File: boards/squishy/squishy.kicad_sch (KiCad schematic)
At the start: 69 parts, among them J10 QXH-060, J2 Conn_02x20_Odd_Even_Shielded, J3 MEM2061-01-188-00-A, J8 TRIGGER, J9 REFCLK, SW2 DFU, U1 LFE5UM5G-45F-8BG381C, U2 GD25Q64EWIGR, U6 ATSAMD09D14A-M, X1 48MHz

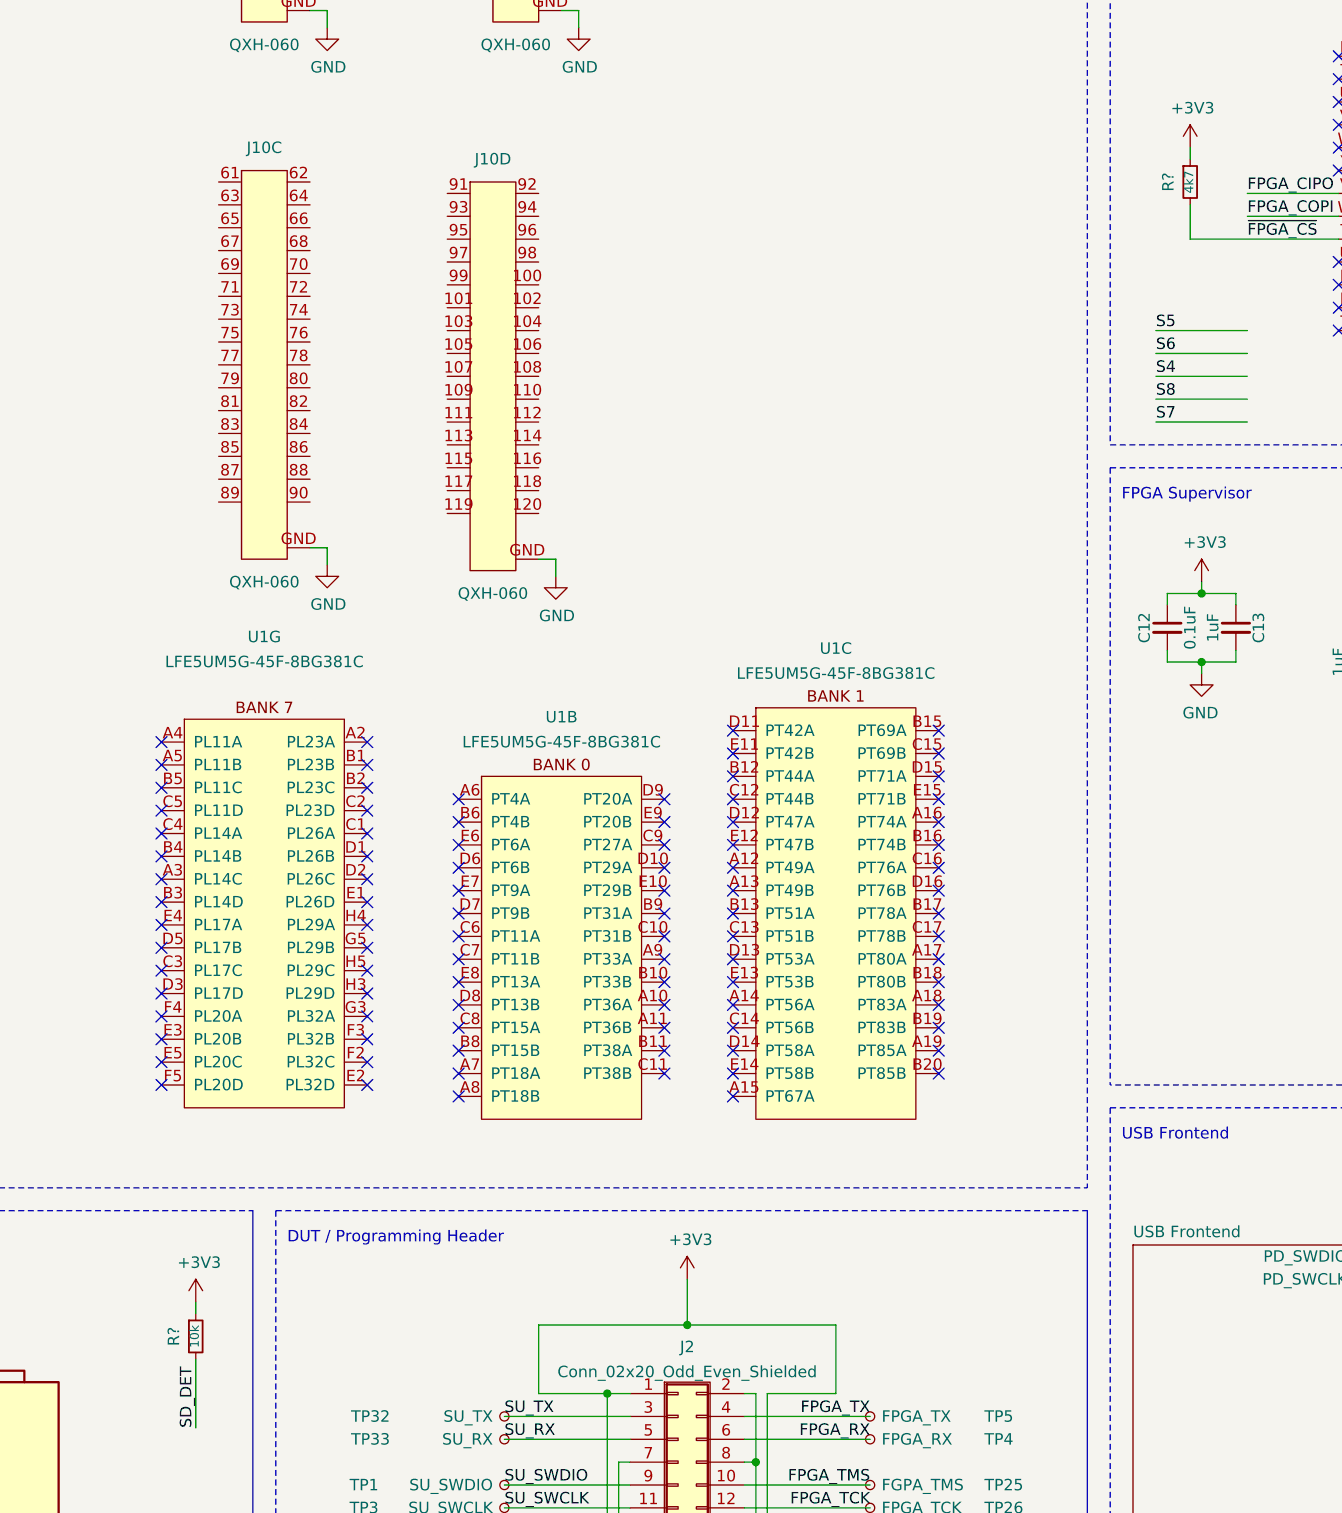
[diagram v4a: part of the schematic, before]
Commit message: hardware: squishy: some footprint/part updates and cleanup
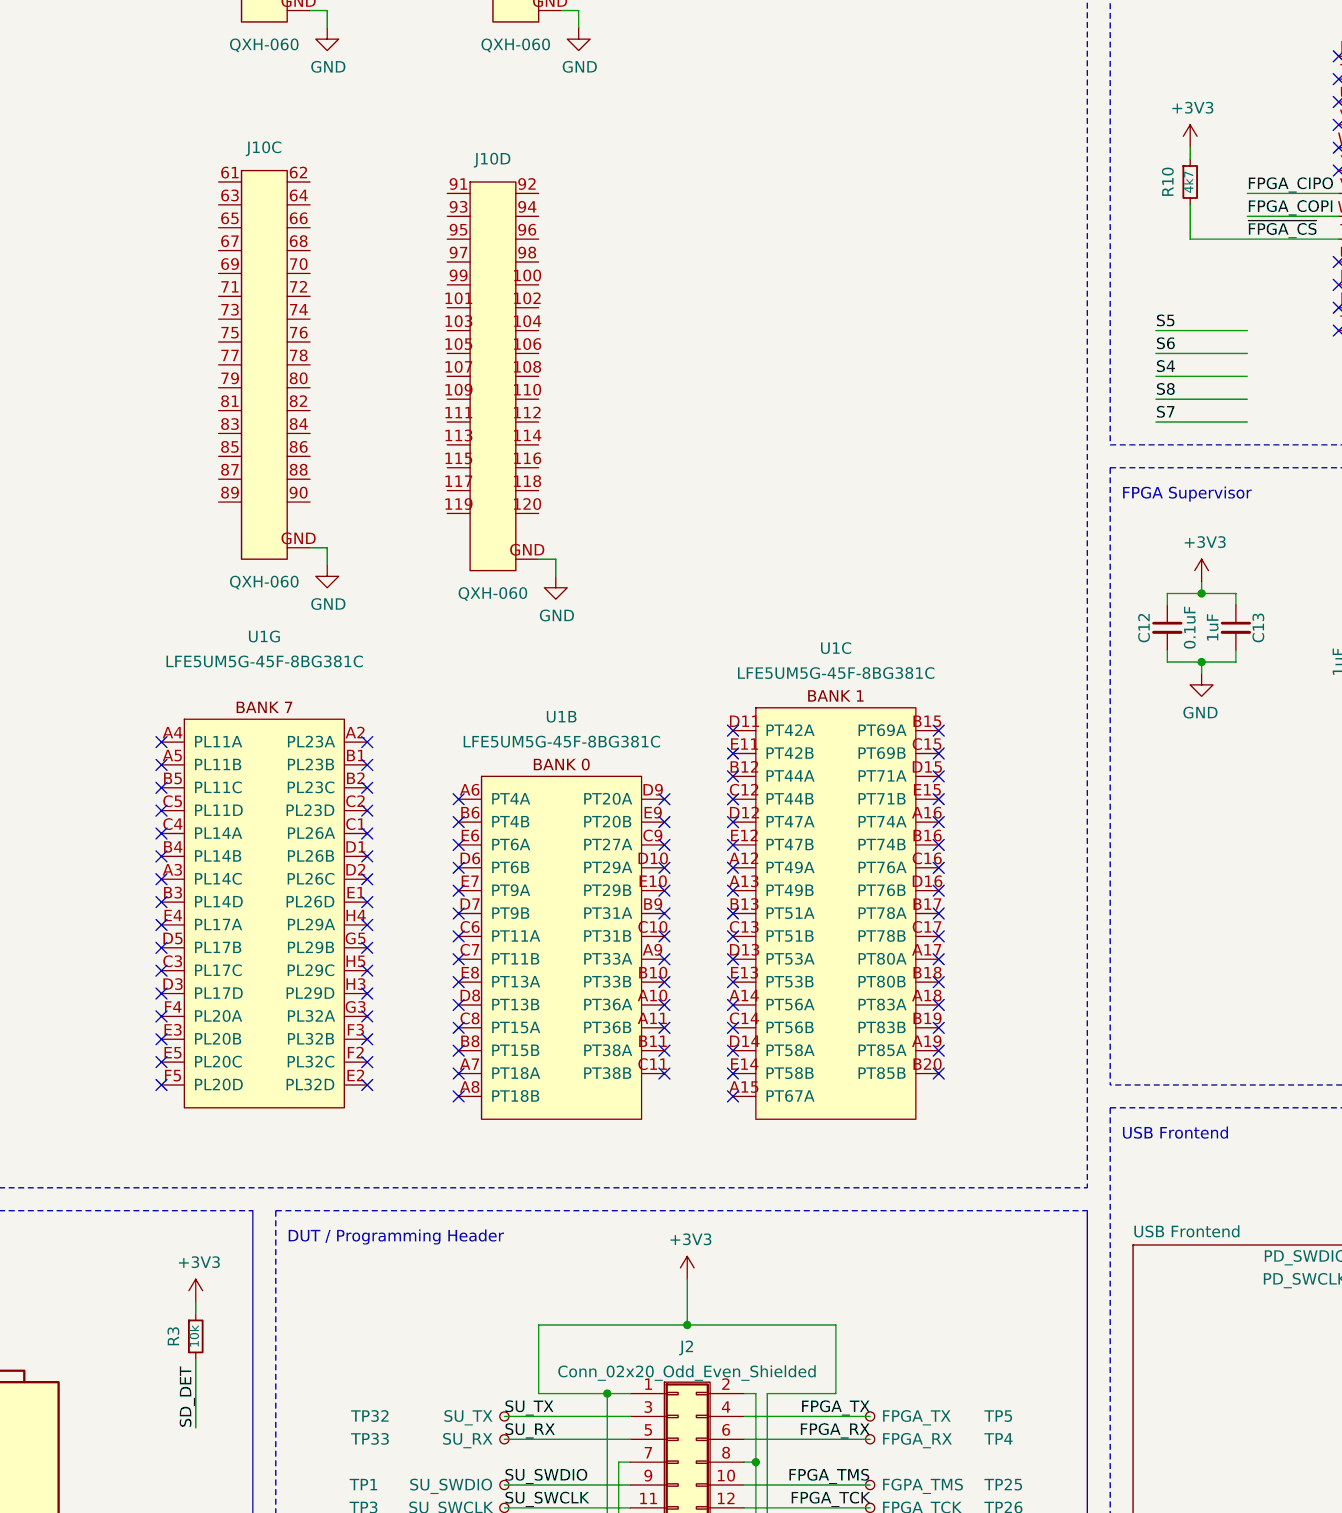
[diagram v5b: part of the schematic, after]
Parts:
- X1: footprint Oscillator:Oscillator_SMD_Abracon_ASE-4Pin_3.2x2.5mm -> rhais_osc:SMD3225
- gave numbers to parts that had none: 2
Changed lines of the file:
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@@
   (symbol (lib_id "power:+3V3") (at 274.32 81.28 0) (unit 1)
     (in_bom yes) (on_board yes)
-    (property "Reference" "#PWR?" (id 0) (at 274.32 85.09 0)
+    (property "Reference" "#PWR0115" (id 0) (at 274.32 85.09 0)
       (effects (font (size 1.27 1.27)) hide)
     )
@@
   (symbol (lib_id "power:GND") (at 83.82 251.46 0) (mirror y) (unit 1)
     (in_bom yes) (on_board yes)
-    (property "Reference" "#PWR?" (id 0) (at 83.82 257.81 0)
+    (property "Reference" "#PWR0158" (id 0) (at 83.82 257.81 0)
       (effects (font (size 1.27 1.27)) hide)
     )
@@
   (symbol (lib_id "Device:R_Small") (at 163.83 213.36 0) (unit 1)
     (in_bom yes) (on_board yes)
-    (property "Reference" "R?" (id 0) (at 161.3916 213.36 90))
+    (property "Reference" "R3" (id 0) (at 161.3916 213.36 90))
     (property "Value" "10k" (id 1) (at 163.703 213.36 90)
       (effects (font (size 1 1)))
@@
   (symbol (lib_id "power:GND") (at 151.13 250.19 0) (mirror y) (unit 1)
     (in_bom yes) (on_board yes)
-    (property "Reference" "#PWR?" (id 0) (at 151.13 256.54 0)
+    (property "Reference" "#PWR0121" (id 0) (at 151.13 256.54 0)
       (effects (font (size 1.27 1.27)) hide)
     )
@@
   (symbol (lib_id "power:+3V3") (at 163.83 209.55 0) (unit 1)
     (in_bom yes) (on_board yes)
-    (property "Reference" "#PWR?" (id 0) (at 163.83 213.36 0)
+    (property "Reference" "#PWR0117" (id 0) (at 163.83 213.36 0)
       (effects (font (size 1.27 1.27)) hide)
     )
@@
       (effects (font (size 1.27 1.27)) (justify left))
     )
-    (property "Footprint" "Oscillator:Oscillator_SMD_Abracon_ASE-4Pin_3.2x2.5mm" (id 2) (at 396.24 29.21 0)
+    (property "Footprint" "rhais_osc:SMD3225" (id 2) (at 396.24 29.21 0)
       (effects (font (size 1.27 1.27)) hide)
     )
@@
   (symbol (lib_id "power:+3V3") (at 83.82 209.55 0) (unit 1)
     (in_bom yes) (on_board yes)
-    (property "Reference" "#PWR?" (id 0) (at 83.82 213.36 0)
+    (property "Reference" "#PWR0159" (id 0) (at 83.82 213.36 0)
       (effects (font (size 1.27 1.27)) hide)
     )
@@
   (symbol (lib_id "Device:R_Small") (at 274.32 85.09 0) (unit 1)
     (in_bom yes) (on_board yes)
-    (property "Reference" "R?" (id 0) (at 271.8816 85.09 90))
+    (property "Reference" "R10" (id 0) (at 271.8816 85.09 90))
     (property "Value" "4k7" (id 1) (at 274.193 85.09 90)
       (effects (font (size 1 1)))
@@
       (reference "#PWR0114") (unit 1) (value "+3V3") (footprint "")
     )
+    (path "/1125f626-31a8-4c15-a457-34bafe0f7a8a"
+      (reference "#PWR0115") (unit 1) (value "+3V3") (footprint "")
+    )
     (path "/135fa4cc-bf68-4ed2-9d1e-cefa9ceb3983/ae01d070-dcbe-48d1-a6bf-bae5c1d66bea"
       (reference "#PWR0116") (unit 1) (value "+2V5") (footprint "")
     )
+    (path "/a6a73655-f18c-45f8-9222-2775c6d60cd7"
+      (reference "#PWR0117") (unit 1) (value "+3V3") (footprint "")
+    )
     (path "/135fa4cc-bf68-4ed2-9d1e-cefa9ceb3983/83c9ce5e-8c50-463e-8693-7640b1cfd54d"
       (reference "#PWR0118") (unit 1) (value "+2V5") (footprint "")
@@
       (reference "#PWR0120") (unit 1) (value "GND") (footprint "")
     )
+    (path "/9db86f43-7048-4d31-878a-5f9d9de3030c"
+      (reference "#PWR0121") (unit 1) (value "GND") (footprint "")
+    )
     (path "/135fa4cc-bf68-4ed2-9d1e-cefa9ceb3983/cd34942c-ad54-4437-ba74-2b44f817dfe1"
       (reference "#PWR0122") (unit 1) (value "+1V2") (footprint "")
@@
       (reference "#PWR0157") (unit 1) (value "+5V") (footprint "")
     )
-    (path "/1125f626-31a8-4c15-a457-34bafe0f7a8a"
-      (reference "#PWR?") (unit 1) (value "+3V3") (footprint "")
-    )
     (path "/201843ce-0114-45ba-8c8c-d6507d3ce53f"
-      (reference "#PWR?") (unit 1) (value "GND") (footprint "")
-    )
-    (path "/9db86f43-7048-4d31-878a-5f9d9de3030c"
-      (reference "#PWR?") (unit 1) (value "GND") (footprint "")
-    )
-    (path "/a6a73655-f18c-45f8-9222-2775c6d60cd7"
-      (reference "#PWR?") (unit 1) (value "+3V3") (footprint "")
+      (reference "#PWR0158") (unit 1) (value "GND") (footprint "")
     )
     (path "/efa27d01-23aa-4804-9887-3774a4e1a8f8"
-      (reference "#PWR?") (unit 1) (value "+3V3") (footprint "")
+      (reference "#PWR0159") (unit 1) (value "+3V3") (footprint "")
     )
     (path "/8f583346-1f09-4133-a8d5-9ebea2335739"
@@
       (reference "R2") (unit 1) (value "10k") (footprint "Resistor_SMD:R_0603_1608Metric")
     )
+    (path "/60333297-0f1e-4367-8965-c6e47559c1c4"
+      (reference "R3") (unit 1) (value "10k") (footprint "Resistor_SMD:R_0603_1608Metric")
+    )
     (path "/00000000-0000-0000-0000-000078041963"
       (reference "R4") (unit 1) (value "4k7") (footprint "Resistor_SMD:R_0603_1608Metric")
@@
       (reference "R9") (unit 1) (value "4k7") (footprint "Resistor_SMD:R_0603_1608Metric")
     )
+    (path "/f59782f8-1313-4c85-8ca3-879016495e5b"
+      (reference "R10") (unit 1) (value "4k7") (footprint "Resistor_SMD:R_0603_1608Metric")
+    )
     (path "/897376f2-0c69-4736-a5dd-4d1ec77915b7/e13c08c5-7ab4-4df6-92fd-05d8877c8155"
       (reference "R11") (unit 1) (value "1M") (footprint "Resistor_SMD:R_0603_1608Metric")
@@
       (reference "R33") (unit 1) (value "10k") (footprint "Resistor_SMD:R_0603_1608Metric")
     )
-    (path "/60333297-0f1e-4367-8965-c6e47559c1c4"
-      (reference "R?") (unit 1) (value "10k") (footprint "Resistor_SMD:R_0603_1608Metric")
-    )
-    (path "/f59782f8-1313-4c85-8ca3-879016495e5b"
-      (reference "R?") (unit 1) (value "4k7") (footprint "Resistor_SMD:R_0603_1608Metric")
-    )
     (path "/135fa4cc-bf68-4ed2-9d1e-cefa9ceb3983/14988e9d-0731-4f35-891c-0cdcce294cdc"
       (reference "SW1") (unit 1) (value "RST") (footprint "lethalbit:SW_Tactile_SPST_Angled_TC-1109DE")
@@
     )
     (path "/b815a8ec-c187-4e06-9203-b853a6ecfa93"
-      (reference "X1") (unit 1) (value "48MHz") (footprint "Oscillator:Oscillator_SMD_Abracon_ASE-4Pin_3.2x2.5mm")
+      (reference "X1") (unit 1) (value "48MHz") (footprint "rhais_osc:SMD3225")
     )
     (path "/897376f2-0c69-4736-a5dd-4d1ec77915b7/9e3a6acb-75f1-42be-91a6-4338c72aea98"
-      (reference "X2") (unit 1) (value "13MHz") (footprint "Oscillator:Oscillator_SMD_Abracon_ASE-4Pin_3.2x2.5mm")
+      (reference "X2") (unit 1) (value "13MHz") (footprint "rhais_osc:SMD3225")
     )
   )
